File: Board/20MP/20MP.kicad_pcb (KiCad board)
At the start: 2 copper layers, 103.2 x 100 mm, 48 parts, among them J1 Conn_01x02_Male, SW1 SHOU_HAN_MSK12C02-HB, SW2 RotaryEncoder_Switch, U1 nice_nanoV2

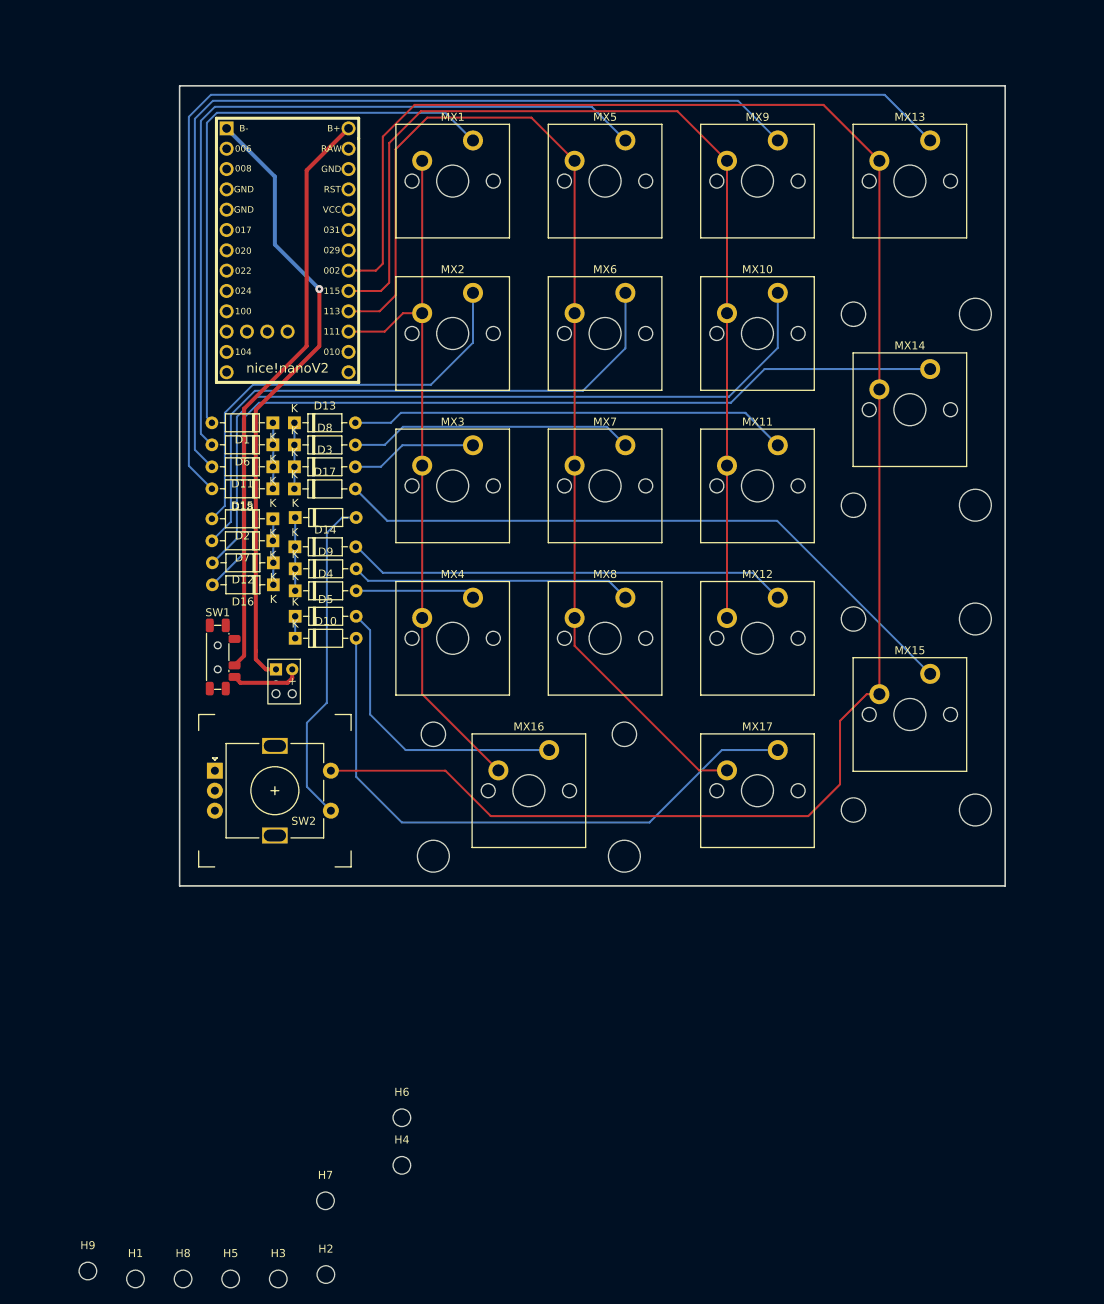
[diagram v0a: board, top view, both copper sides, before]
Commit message: removed old tracks
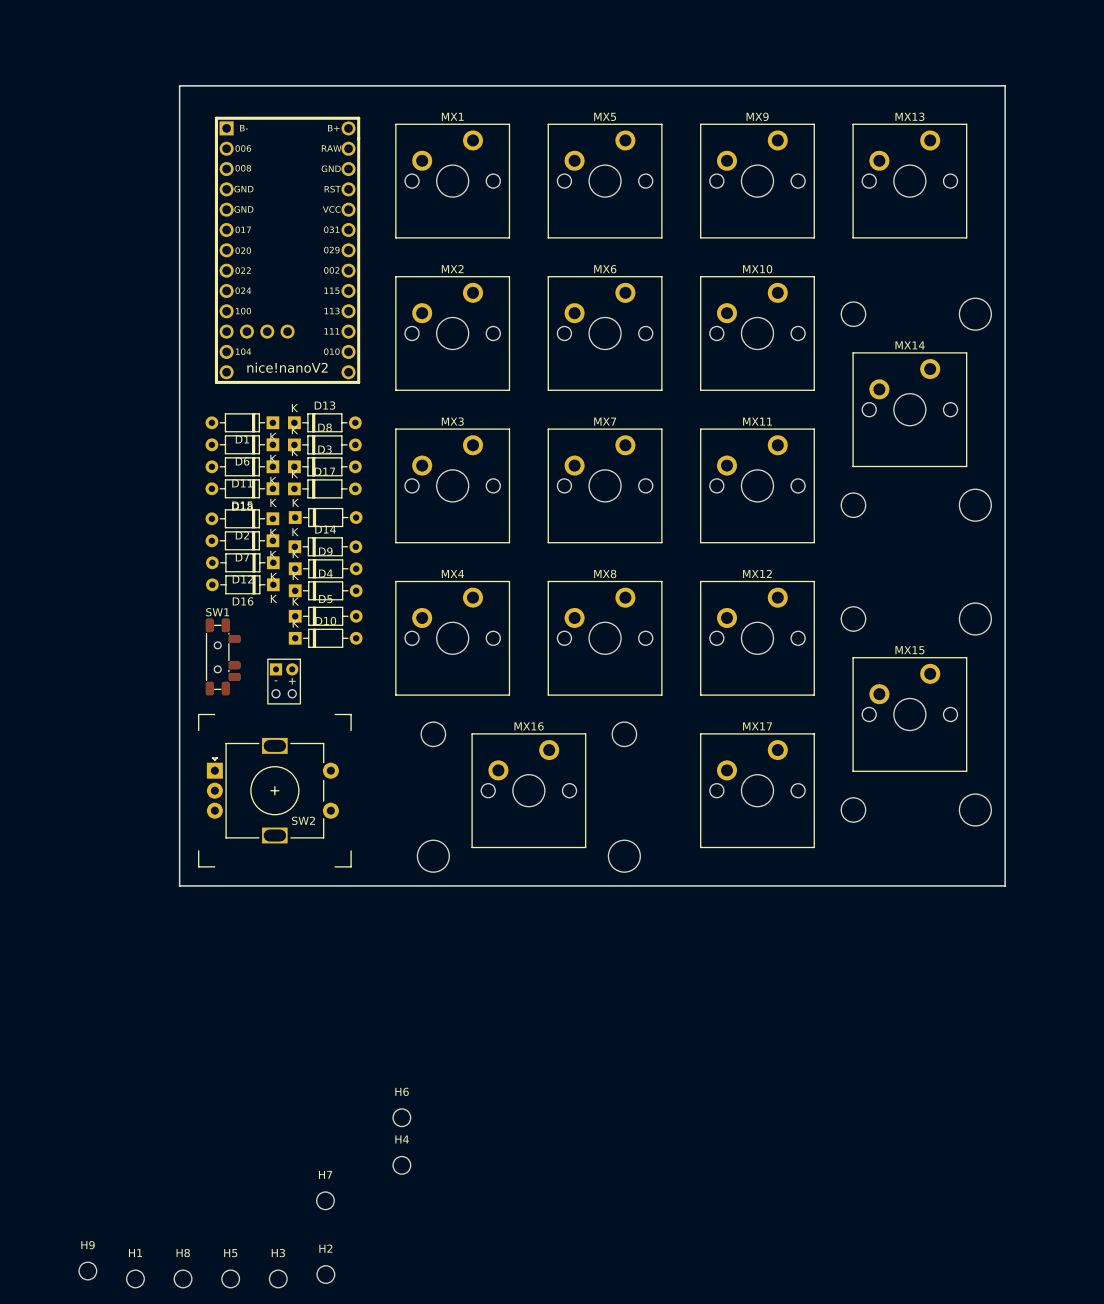
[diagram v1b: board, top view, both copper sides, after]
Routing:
- net COL3: track 235.7 -> 0.00 mm
- net Net-(D15-Pad2): track 143.9 -> 0.00 mm
- net COL1: track 137.4 -> 0.00 mm
- net COL2: track 126.6 -> 0.00 mm
- net Net-(D11-Pad2): track 120.2 -> 0.00 mm
- net Net-(D16-Pad2): track 110.8 -> 0.00 mm
- net Net-(D12-Pad2): track 97.6 -> 0.00 mm
- net Net-(D6-Pad2): track 96.6 -> 0.00 mm
- net COL0: track 90.9 -> 0.00 mm
- net Net-(D17-Pad2): track 81.4 -> 0.00 mm
- net B-: track 77.5 -> 0.00 mm, vias 1 -> 0
- net Net-(D7-Pad2): track 76.4 -> 0.00 mm
- net Net-(D10-Pad2): track 76.1 -> 0.00 mm
- net B+: track 73.0 -> 0.00 mm
- net Net-(D1-Pad2): track 73.0 -> 0.00 mm
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
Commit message: added nice view
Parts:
- added Display1: nice!view, microcontroller:nice_view, F.Cu at (37.5, 93.0)
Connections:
- U1 pad 10: unconnected-(U1-Pad10) -> SCK
- U1 pad 11: unconnected-(U1-Pad11) -> CS
- U1 pad 9: unconnected-(U1-Pad9) -> MOSI
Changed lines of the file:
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@@
   (net 21 "Net-(D16-Pad2)")
   (net 22 "Net-(D17-Pad2)")
-  (net 23 "Net-(SW2-PadS1)")
+  (net 23 "Net-(D18-Pad2)")
   (net 24 "B-")
   (net 25 "Net-(J1-Pad2)")
@@
   (net 33 "/ROT_1A")
   (net 34 "/ROT_1B")
-  (net 35 "unconnected-(U1-Pad9)")
-  (net 36 "unconnected-(U1-Pad10)")
-  (net 37 "unconnected-(U1-Pad11)")
+  (net 35 "MOSI")
+  (net 36 "SCK")
+  (net 37 "CS")
   (net 38 "unconnected-(U1-Pad12)")
   (net 39 "unconnected-(U1-Pad13)")
@@
       (net 7 "ROW3") (pinfunction "K") (pintype "passive"))
     (pad "2" thru_hole oval (at 7.62 0) (size 1.6 1.6) (drill 0.8) (layers *.Cu *.Mask)
-      (net 23 "Net-(SW2-PadS1)") (pinfunction "A") (pintype "passive"))
+      (net 23 "Net-(D18-Pad2)") (pinfunction "A") (pintype "passive"))
     (model "${KICAD6_3DMODEL_DIR}/Diode_THT.3dshapes/D_DO-35_SOD27_P7.62mm_Horizontal.wrl"
       (offset (xyz 0 0 0))
@@
       (rotate (xyz 0 0 0))
     )
+  )
+  (footprint "microcontroller:nice_view" (layer "F.Cu")
+    (at 37.55 93.05)
+    (property "Sheetfile" "20MP.kicad_sch")
+    (property "Sheetname" "")
+    (attr through_hole)
+    (fp_text reference "Display1" (at 0 1.27 unlocked) (layer "F.Fab")
+      (effects (font (size 1 1) (thickness 0.15)))
+    )
+    (fp_text value "nice!view" (at 0 21.59 unlocked) (layer "F.SilkS")
+      (effects (font (size 1 1) (thickness 0.15)))
+    )
+    (fp_text user "VCC" (at 0 17.78 90 unlocked) (layer "F.SilkS")
+      (effects (font (size 1 1) (thickness 0.15)) (justify right))
+    )
+    (fp_text user "CS" (at 5.08 17.78 90 unlocked) (layer "F.SilkS")
+      (effects (font (size 1 1) (thickness 0.15)) (justify right))
+    )
+    (fp_text user "GND" (at 2.54 17.78 90 unlocked) (layer "F.SilkS")
+      (effects (font (size 1 1) (thickness 0.15)) (justify right))
+    )
+    (fp_text user "MOSI" (at -5.08 17.78 90 unlocked) (layer "F.SilkS")
+      (effects (font (size 1 1) (thickness 0.15)) (justify right))
+    )
+    (fp_text user "SCK" (at -2.54 17.78 90 unlocked) (layer "F.SilkS")
+      (effects (font (size 1 1) (thickness 0.15)) (justify right))
+    )
+    (fp_text user "${REFERENCE}" (at 0 4 unlocked) (layer "F.Fab") hide
+      (effects (font (size 1 1) (thickness 0.15)))
+    )
+    (fp_rect (start -6.35 15.24) (end 6.35 17.78) (layer "F.SilkS") (width 0.12) (fill none))
+    (fp_rect (start 7 17.78) (end -7 -18.22) (layer "F.Fab") (width 0.12) (fill none))
+    (pad "1" thru_hole circle (at -5.08 16.51) (size 1.7526 1.7526) (drill 1.0922) (layers *.Cu *.Mask)
+      (net 35 "MOSI") (pinfunction "MOSI") (pintype "input"))
+    (pad "2" thru_hole circle (at -2.54 16.51) (size 1.7526 1.7526) (drill 1.0922) (layers *.Cu *.Mask)
+      (net 36 "SCK") (pinfunction "SCK") (pintype "input"))
+    (pad "3" thru_hole circle (at 0 16.51) (size 1.7526 1.7526) (drill 1.0922) (layers *.Cu *.Mask)
+      (net 43 "VCC") (pinfunction "VCC") (pintype "power_in"))
+    (pad "4" thru_hole circle (at 2.54 16.51) (size 1.7526 1.7526) (drill 1.0922) (layers *.Cu *.Mask)
+      (net 32 "GND") (pinfunction "GND") (pintype "power_out"))
+    (pad "5" thru_hole circle (at 5.08 16.51) (size 1.7526 1.7526) (drill 1.0922) (layers *.Cu *.Mask)
+      (net 37 "CS") (pinfunction "CS") (pintype "passive"))
   )
   (footprint "mx-switches:CherryMX-2.00U" (layer "F.Cu")
@@
       (net 9 "ROW4") (pinfunction "P0.22") (pintype "output"))
     (pad "9" thru_hole circle (at 3.81 7.62 270) (size 1.7526 1.7526) (drill 1.0922) (layers *.Cu *.SilkS *.Mask)
-      (net 35 "unconnected-(U1-Pad9)") (pinfunction "P0.24") (pintype "output"))
+      (net 35 "MOSI") (pinfunction "P0.24") (pintype "output"))
     (pad "10" thru_hole circle (at 6.35 7.62 270) (size 1.7526 1.7526) (drill 1.0922) (layers *.Cu *.SilkS *.Mask)
-      (net 36 "unconnected-(U1-Pad10)") (pinfunction "P1.00") (pintype "output"))
+      (net 36 "SCK") (pinfunction "P1.00") (pintype "output"))
     (pad "11" thru_hole circle (at 8.89 7.62 270) (size 1.7526 1.7526) (drill 1.0922) (layers *.Cu *.SilkS *.Mask)
-      (net 37 "unconnected-(U1-Pad11)") (pinfunction "P0.11") (pintype "output"))
+      (net 37 "CS") (pinfunction "P0.11") (pintype "output"))
     (pad "12" thru_hole circle (at 11.43 7.62 270) (size 1.7526 1.7526) (drill 1.0922) (layers *.Cu *.SilkS *.Mask)
       (net 38 "unconnected-(U1-Pad12)") (pinfunction "P1.04") (pintype "output"))
@@
     (pad "MP" thru_hole rect (at 0 -5.6) (size 3.2 2) (drill oval 2.8 1.5) (layers *.Cu *.Mask))
     (pad "S1" thru_hole circle (at 7 2.5) (size 2 2) (drill 1) (layers *.Cu *.Mask)
-      (net 23 "Net-(SW2-PadS1)") (pinfunction "S1") (pintype "passive"))
+      (net 23 "Net-(D18-Pad2)") (pinfunction "S1") (pintype "passive"))
     (pad "S2" thru_hole circle (at 7 -2.5) (size 2 2) (drill 1) (layers *.Cu *.Mask)
       (net 29 "COL3") (pinfunction "S2") (pintype "passive"))

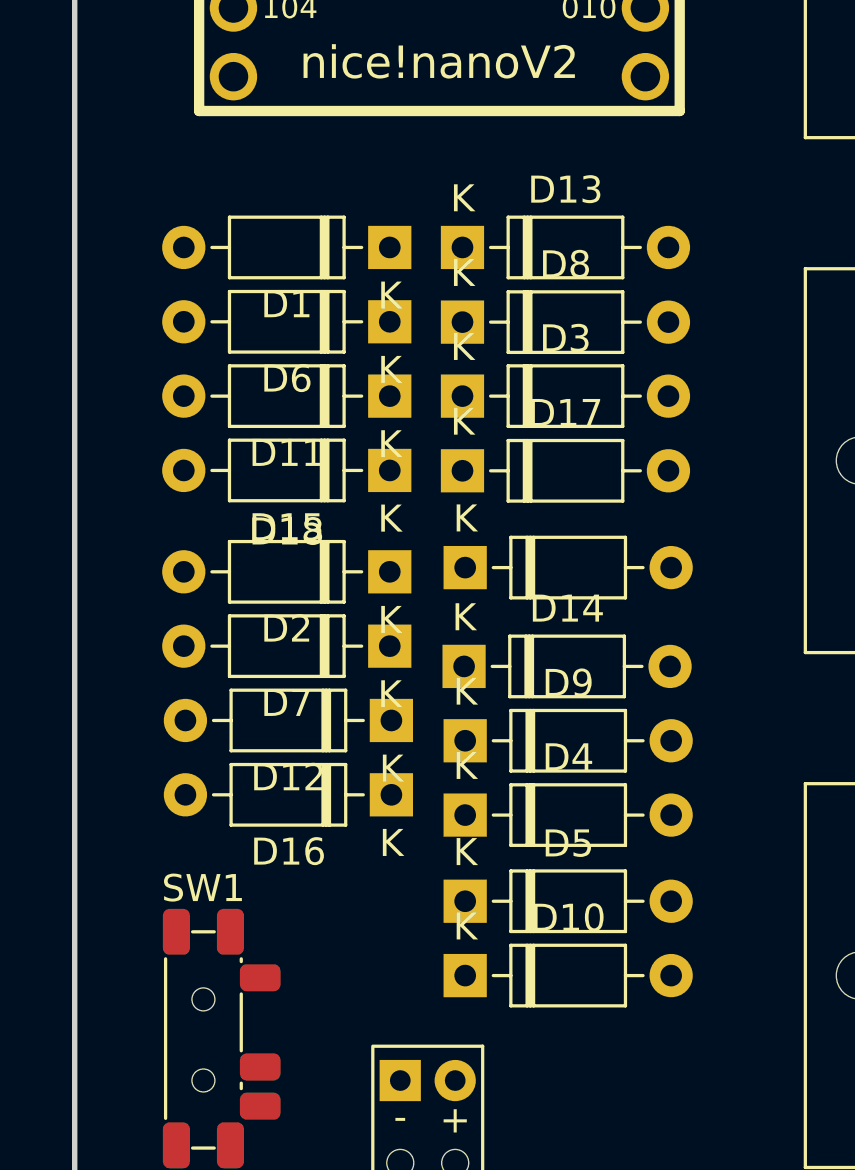
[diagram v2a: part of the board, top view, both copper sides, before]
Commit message: changed diodes to smd
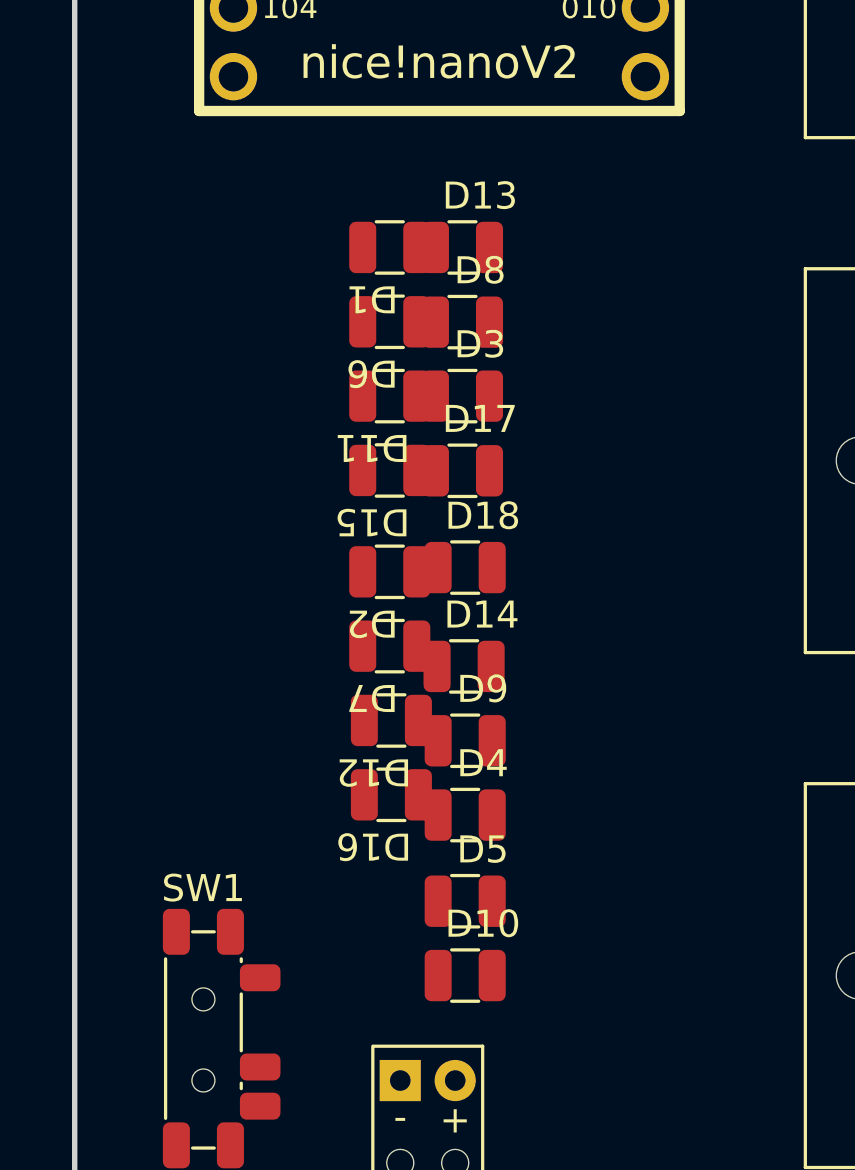
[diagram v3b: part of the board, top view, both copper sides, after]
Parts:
- D1, D10, D11, D12, D13, D14, D15, D16, D17, D18, D2, D3, D4, D5, D6, D7, D8, D9: footprint Diode_THT:D_DO-35_SOD27_P7.62mm_Horizontal -> led:led_capacitor
